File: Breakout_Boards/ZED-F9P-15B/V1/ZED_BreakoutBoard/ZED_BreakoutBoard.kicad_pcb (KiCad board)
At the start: 2 copper layers, 15 parts, among them IC1 ZED-F9P-15B, J1 RF2-04A-T-00-50-G, J2 GPS_Conn_02x04_Top_Bottom

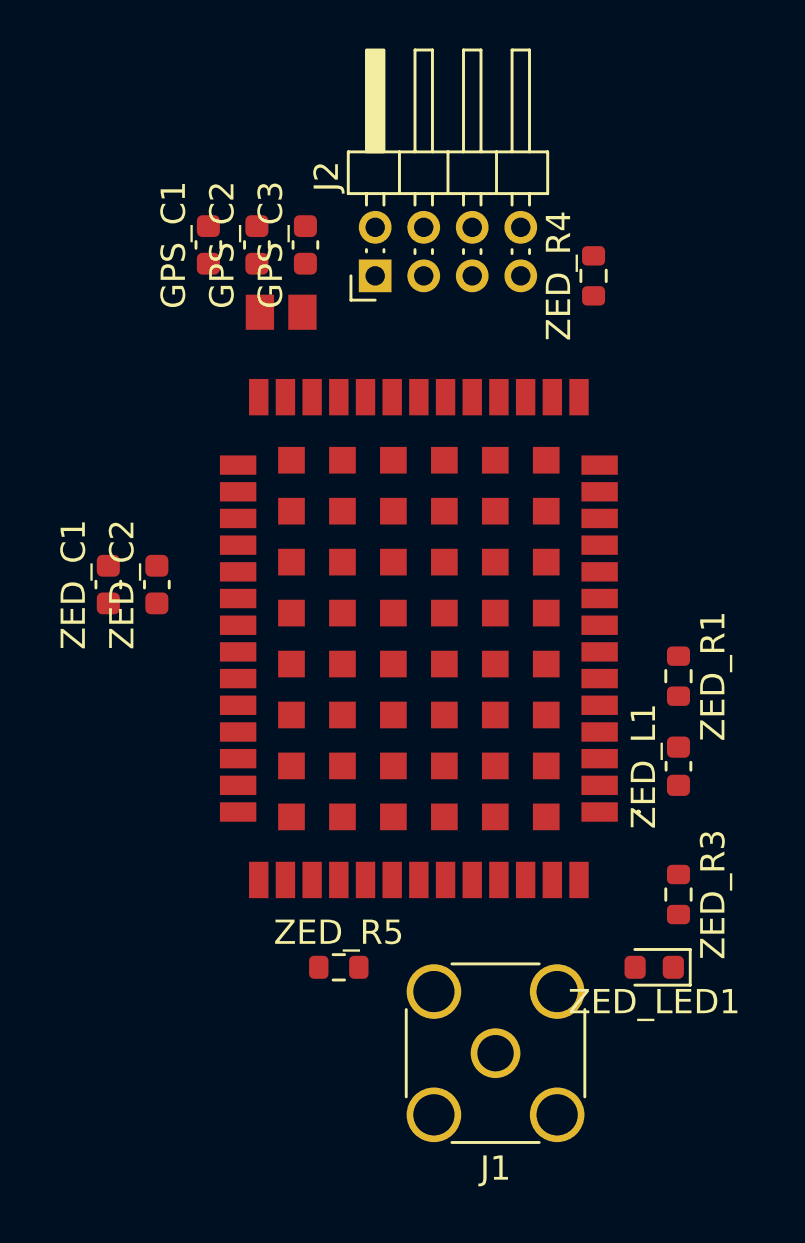
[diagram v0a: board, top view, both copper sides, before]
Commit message: fix: gnd connection, pcb approximative edge
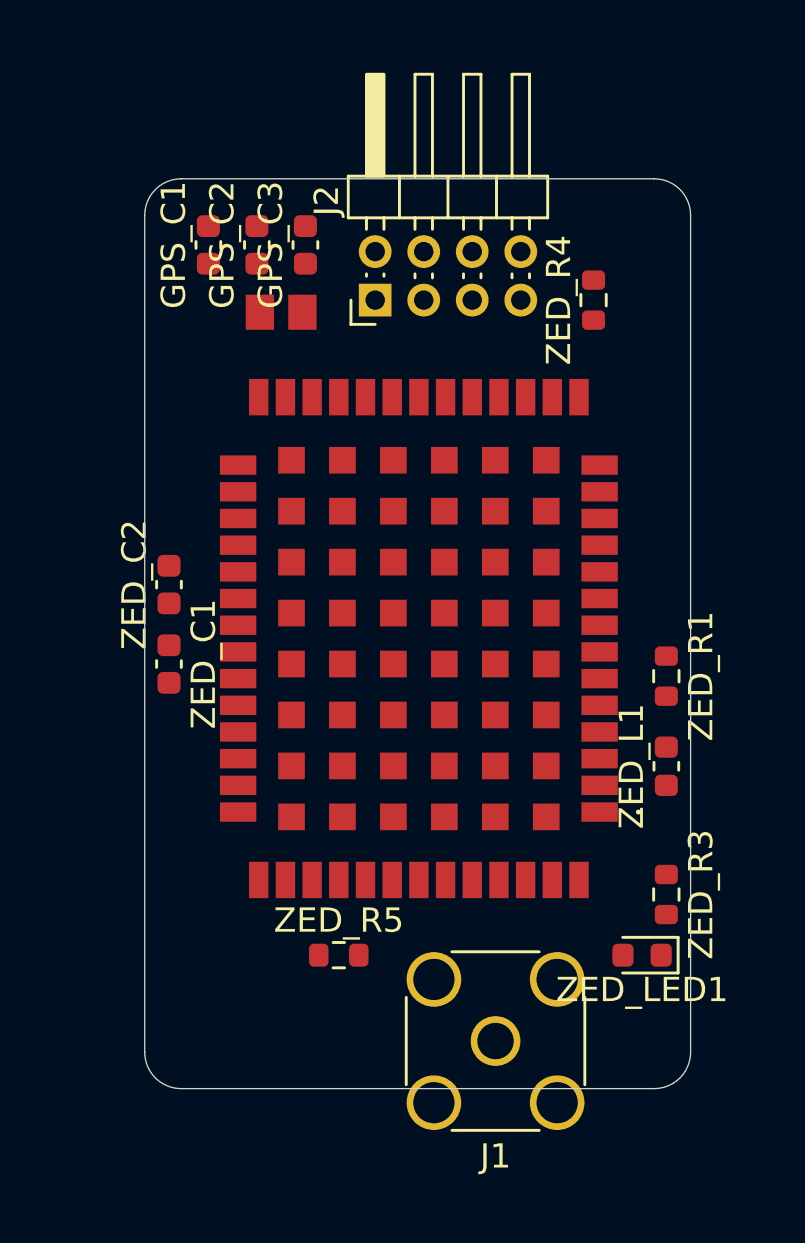
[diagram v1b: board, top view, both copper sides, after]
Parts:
- moved ZED_C1 4.12 mm to (122.0, 87.5), turned to -90 degrees
- moved J2 1.00 mm to (130.5, 72.5)
- moved ZED_R4 1.00 mm to (139.5, 72.5)
- moved ZED_LED1 0.71 mm to (141.5, 99.5)
- moved J1 0.50 mm to (135.5, 103.0)
- moved ZED_C2 0.50 mm to (122.0, 84.2)
- moved ZED_L1 0.50 mm to (142.5, 91.7)
- moved ZED_R1 0.50 mm to (142.5, 88.0)
- moved ZED_R3 0.50 mm to (142.5, 97.0)
- moved ZED_R5 0.50 mm to (129.0, 99.5)
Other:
- board outline added: 22.5 x 37.5 mm
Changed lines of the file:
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@@
 	(footprint "Resistor_SMD:R_0603_1608Metric"
 		(layer "F.Cu")
-		(at 129 100)
+		(at 129 99.5)
 		(descr "Resistor SMD 0603 (1608 Metric), square (rectangular) end terminal, IPC-7351 nominal, (Body size source: IPC-SM-782 page 72, https://www.pcb-3d.com/wordpress/wp-content/uploads/ipc-sm-782a_amendment_1_and_2.pdf), generated with kicad-footprint-generator")
 		(tags "resistor")
@@
 	(footprint "LED_SMD:LED_0603_1608Metric"
 		(layer "F.Cu")
-		(at 142 100 180)
+		(at 141.5 99.5 180)
 		(descr "LED SMD 0603 (1608 Metric), square (rectangular) end terminal, IPC-7351 nominal, (Body size source: http://www.tortai-tech.com/upload/download/2011102023233369053.pdf), generated with kicad-footprint-generator")
 		(tags "LED")
@@
 	(footprint "Resistor_SMD:R_0603_1608Metric"
 		(layer "F.Cu")
-		(at 143 97 -90)
+		(at 142.5 97 -90)
 		(descr "Resistor SMD 0603 (1608 Metric), square (rectangular) end terminal, IPC-7351 nominal, (Body size source: IPC-SM-782 page 72, https://www.pcb-3d.com/wordpress/wp-content/uploads/ipc-sm-782a_amendment_1_and_2.pdf), generated with kicad-footprint-generator")
 		(tags "resistor")
@@
 	(footprint "Resistor_SMD:R_0603_1608Metric"
 		(layer "F.Cu")
-		(at 143 88 -90)
+		(at 142.5 88 -90)
 		(descr "Resistor SMD 0603 (1608 Metric), square (rectangular) end terminal, IPC-7351 nominal, (Body size source: IPC-SM-782 page 72, https://www.pcb-3d.com/wordpress/wp-content/uploads/ipc-sm-782a_amendment_1_and_2.pdf), generated with kicad-footprint-generator")
 		(tags "resistor")
@@
 	(footprint "Connector_Coaxial:SMA_Wurth_60312002114503_Vertical"
 		(layer "F.Cu")
-		(at 135.46 103.54 180)
+		(at 135.46 103.04 180)
 		(descr "https://www.we-online.de/katalog/datasheet/60312002114503.pdf")
 		(tags "SMA THT Female Jack Vertical ExtendedLegs")
@@
 	(footprint "Inductor_SMD:L_0603_1608Metric"
 		(layer "F.Cu")
-		(at 143 91.7125 90)
+		(at 142.5 91.7125 90)
 		(descr "Inductor SMD 0603 (1608 Metric), square (rectangular) end terminal, IPC-7351 nominal, (Body size source: http://www.tortai-tech.com/upload/download/2011102023233369053.pdf), generated with kicad-footprint-generator")
 		(tags "inductor")
@@
 	(footprint "Capacitor_SMD:C_0603_1608Metric"
 		(layer "F.Cu")
-		(at 119.5 84.225 90)
+		(at 122 87.5 -90)
 		(descr "Capacitor SMD 0603 (1608 Metric), square (rectangular) end terminal, IPC-7351 nominal, (Body size source: IPC-SM-782 page 76, https://www.pcb-3d.com/wordpress/wp-content/uploads/ipc-sm-782a_amendment_1_and_2.pdf), generated with kicad-footprint-generator")
 		(tags "capacitor")
@@
 		(attr smd)
 		(fp_line
-			(start -0.14058 -0.51)
-			(end 0.14058 -0.51)
+			(start -0.14058 0.51)
+			(end 0.14058 0.51)
 			(stroke
 				(width 0.12)
@@
 		)
 		(fp_line
-			(start -0.14058 0.51)
-			(end 0.14058 0.51)
+			(start -0.14058 -0.51)
+			(end 0.14058 -0.51)
 			(stroke
 				(width 0.12)
@@
 		)
 		(fp_line
-			(start 1.48 -0.73)
-			(end 1.48 0.73)
+			(start -1.48 0.73)
+			(end -1.48 -0.73)
 			(stroke
 				(width 0.05)
@@
 		)
 		(fp_line
-			(start -1.48 -0.73)
-			(end 1.48 -0.73)
+			(start 1.48 0.73)
+			(end -1.48 0.73)
 			(stroke
 				(width 0.05)
@@
 		)
 		(fp_line
-			(start 1.48 0.73)
-			(end -1.48 0.73)
+			(start -1.48 -0.73)
+			(end 1.48 -0.73)
 			(stroke
 				(width 0.05)
@@
 		)
 		(fp_line
-			(start -1.48 0.73)
-			(end -1.48 -0.73)
+			(start 1.48 -0.73)
+			(end 1.48 0.73)
 			(stroke
 				(width 0.05)
@@
 		)
 		(fp_line
-			(start 0.8 -0.4)
-			(end 0.8 0.4)
+			(start -0.8 0.4)
+			(end -0.8 -0.4)
 			(stroke
 				(width 0.1)
@@
 		)
 		(fp_line
-			(start -0.8 -0.4)
-			(end 0.8 -0.4)
+			(start 0.8 0.4)
+			(end -0.8 0.4)
 			(stroke
 				(width 0.1)
@@
 		)
 		(fp_line
-			(start 0.8 0.4)
-			(end -0.8 0.4)
+			(start -0.8 -0.4)
+			(end 0.8 -0.4)
 			(stroke
 				(width 0.1)
@@
 		)
 		(fp_line
-			(start -0.8 0.4)
-			(end -0.8 -0.4)
+			(start 0.8 -0.4)
+			(end 0.8 0.4)
 			(stroke
 				(width 0.1)
@@
 		)
 		(pad "1" smd roundrect
-			(at -0.775 0 90)
+			(at -0.775 0 270)
 			(size 0.9 0.95)
 			(layers "F.Cu" "F.Mask" "F.Paste")
@@
 		)
 		(pad "2" smd roundrect
-			(at 0.775 0 90)
+			(at 0.775 0 270)
 			(size 0.9 0.95)
 			(layers "F.Cu" "F.Mask" "F.Paste")
@@
 	(footprint "Capacitor_SMD:C_0603_1608Metric"
 		(layer "F.Cu")
-		(at 121.5 84.225 90)
+		(at 122 84.225 90)
 		(descr "Capacitor SMD 0603 (1608 Metric), square (rectangular) end terminal, IPC-7351 nominal, (Body size source: IPC-SM-782 page 76, https://www.pcb-3d.com/wordpress/wp-content/uploads/ipc-sm-782a_amendment_1_and_2.pdf), generated with kicad-footprint-generator")
 		(tags "capacitor")
@@
 	(footprint "Connector_PinHeader_2.00mm:PinHeader_2x04_P2.00mm_Horizontal"
 		(layer "F.Cu")
-		(at 130.5 71.5 90)
+		(at 130.5 72.5 90)
 		(descr "Through hole angled pin header, 2x04, 2.00mm pitch, 4.2mm pin length, double rows")
 		(tags "Through hole angled pin header THT 2x04 2.00mm double row")
@@
 	(footprint "Resistor_SMD:R_0603_1608Metric"
 		(layer "F.Cu")
-		(at 139.5 71.5 90)
+		(at 139.5 72.5 90)
 		(descr "Resistor SMD 0603 (1608 Metric), square (rectangular) end terminal, IPC-7351 nominal, (Body size source: IPC-SM-782 page 72, https://www.pcb-3d.com/wordpress/wp-content/uploads/ipc-sm-782a_amendment_1_and_2.pdf), generated with kicad-footprint-generator")
 		(tags "resistor")
@@
 		)
 	)
+	(gr_arc
+		(start 122.5 105)
+		(mid 121.43934 104.56066)
+		(end 121 103.5)
+		(stroke
+			(width 0.05)
+			(type default)
+		)
+		(layer "Edge.Cuts")
+	)
+	(gr_line
+		(start 122.5 67.5)
+		(end 142 67.5)
+		(stroke
+			(width 0.05)
+			(type default)
+		)
+		(layer "Edge.Cuts")
+	)
+	(gr_line
+		(start 143.5 69)
+		(end 143.5 103.5)
+		(stroke
+			(width 0.05)
+			(type default)
+		)
+		(layer "Edge.Cuts")
+	)
+	(gr_arc
+		(start 121 69)
+		(mid 121.43934 67.93934)
+		(end 122.5 67.5)
+		(stroke
+			(width 0.05)
+			(type default)
+		)
+		(layer "Edge.Cuts")
+	)
+	(gr_line
+		(start 142 105)
+		(end 122.5 105)
+		(stroke
+			(width 0.05)
+			(type default)
+		)
+		(layer "Edge.Cuts")
+	)
+	(gr_arc
+		(start 143.5 103.5)
+		(mid 143.06066 104.56066)
+		(end 142 105)
+		(stroke
+			(width 0.05)
+			(type default)
+		)
+		(layer "Edge.Cuts")
+	)
+	(gr_arc
+		(start 142 67.5)
+		(mid 143.06066 67.93934)
+		(end 143.5 69)
+		(stroke
+			(width 0.05)
+			(type default)
+		)
+		(layer "Edge.Cuts")
+	)
+	(gr_line
+		(start 121 103.5)
+		(end 121 69)
+		(stroke
+			(width 0.05)
+			(type default)
+		)
+		(layer "Edge.Cuts")
+	)
 	(embedded_fonts no)

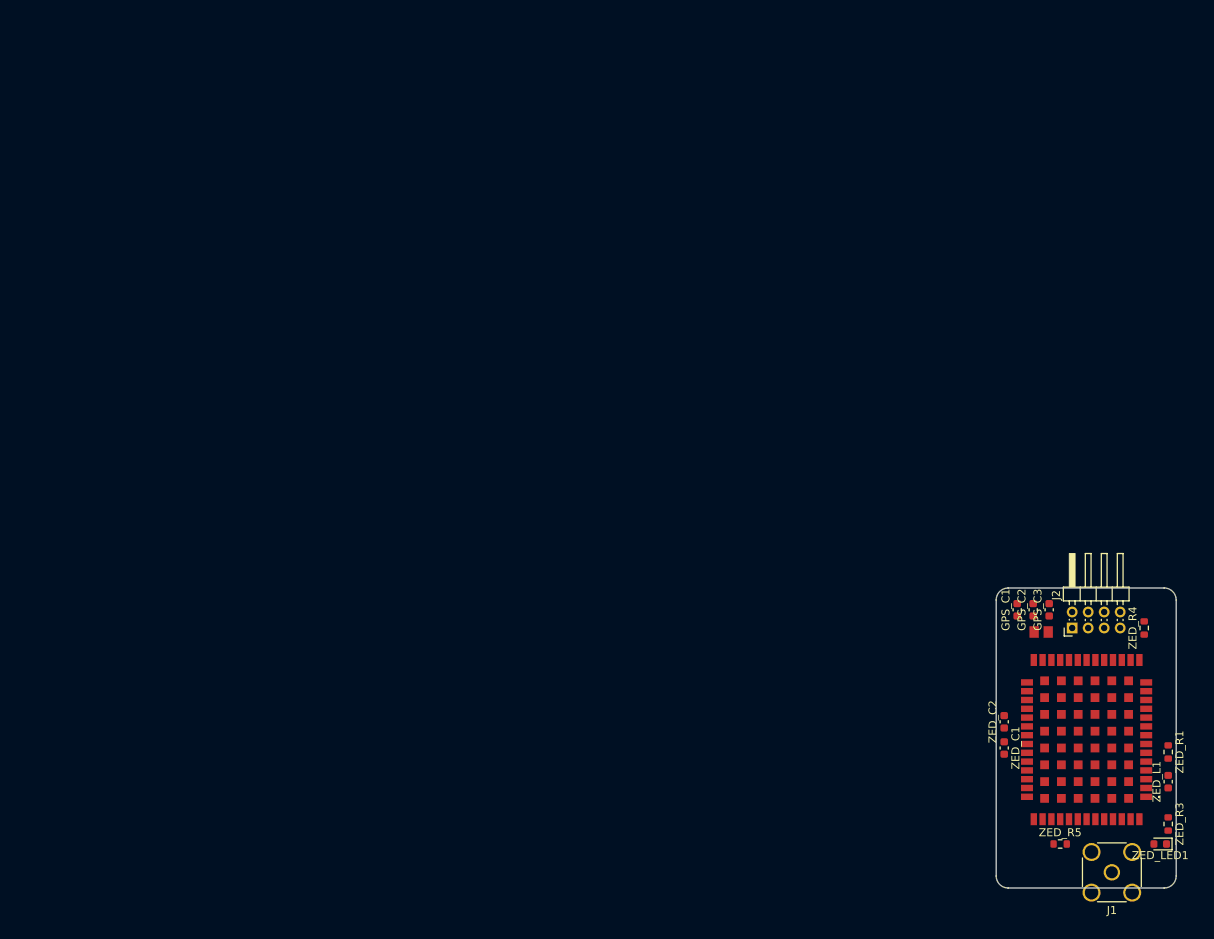
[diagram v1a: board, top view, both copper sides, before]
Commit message: feat edge pcb sma, add edge pcb layout
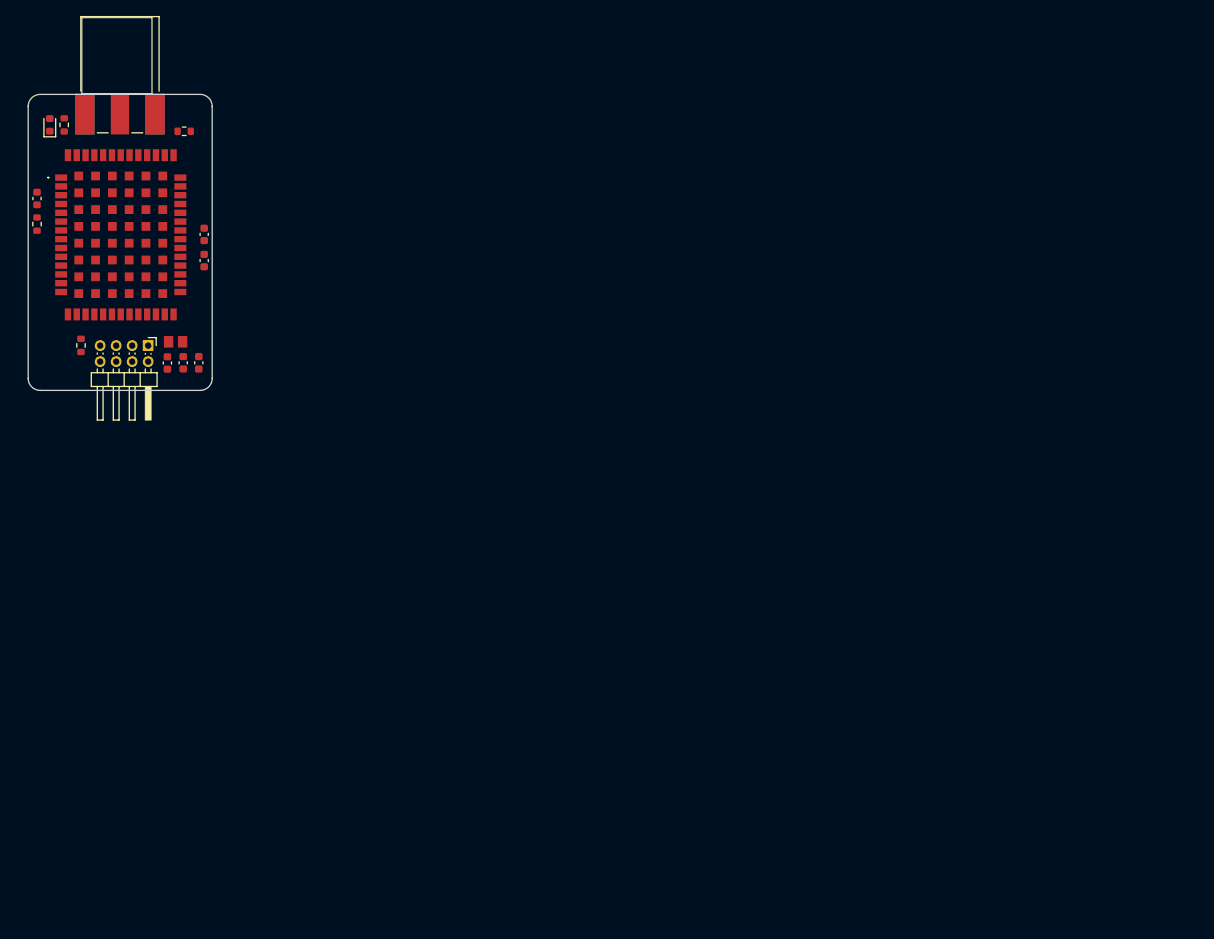
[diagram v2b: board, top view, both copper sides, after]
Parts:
- J1: value RF2-04A-T-00-50-G -> 142-0701-801; footprint Connector_Coaxial:SMA_Wurth_60312002114503_Vertical -> ZED_Library:CONN_142-0701-801
- moved ZED_LED1 165.4 mm to (2.70, 9.61), turned to 90 degrees
- moved ZED_R3 163.3 mm to (4.50, 9.61), turned to 90 degrees
- moved ZED_L1 159.1 mm to (1.10, 18.8), turned to -90 degrees
- moved J1 156.1 mm to (11.5, 8.27), turned to 0 degrees
- moved ZED_R1 156.0 mm to (1.10, 22.0), turned to 90 degrees
- moved ZED_R5 141.2 mm to (19.5, 10.4), turned to 180 degrees
- moved ZED_R4 137.5 mm to (6.60, 37.2), turned to -90 degrees
- moved IC1 136.2 mm to (11.6, 23.4), turned to -90 degrees
- moved J2 120.8 mm to (15.0, 37.2), turned to -90 degrees
- moved ZED_C1 118.8 mm to (22.0, 23.3), turned to 90 degrees
- moved ZED_C2 115.4 mm to (22.0, 26.6), turned to -90 degrees
- moved GPS_C3 114.5 mm to (17.4, 39.4), turned to -90 degrees
- moved GPS_FB1 114.1 mm to (18.4, 36.7), turned to 0 degrees
- moved GPS_C2 110.6 mm to (19.4, 39.4), turned to -90 degrees
- moved GPS_C1 106.9 mm to (21.3, 39.4), turned to -90 degrees
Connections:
- IC1 pad 49: GPS_GND -> Net-(IC1-RESET_N)
- J2 pad 6: ZED_EXTINT -> GPS_GND
- J2 pad 7: GPS_GND -> ZED_EXTINT
- J2 pad 8: GPS_GND -> Net-(J2-Pin_8)
- ZED_R4 pad 2: GPS_GND -> Net-(J2-Pin_8)
- ZED_R5 pad 2: GPS_GND -> Net-(IC1-RESET_N)
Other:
- board size 22.5 x 37.5 mm -> 23 x 37 mm
- board text added: "VCC"

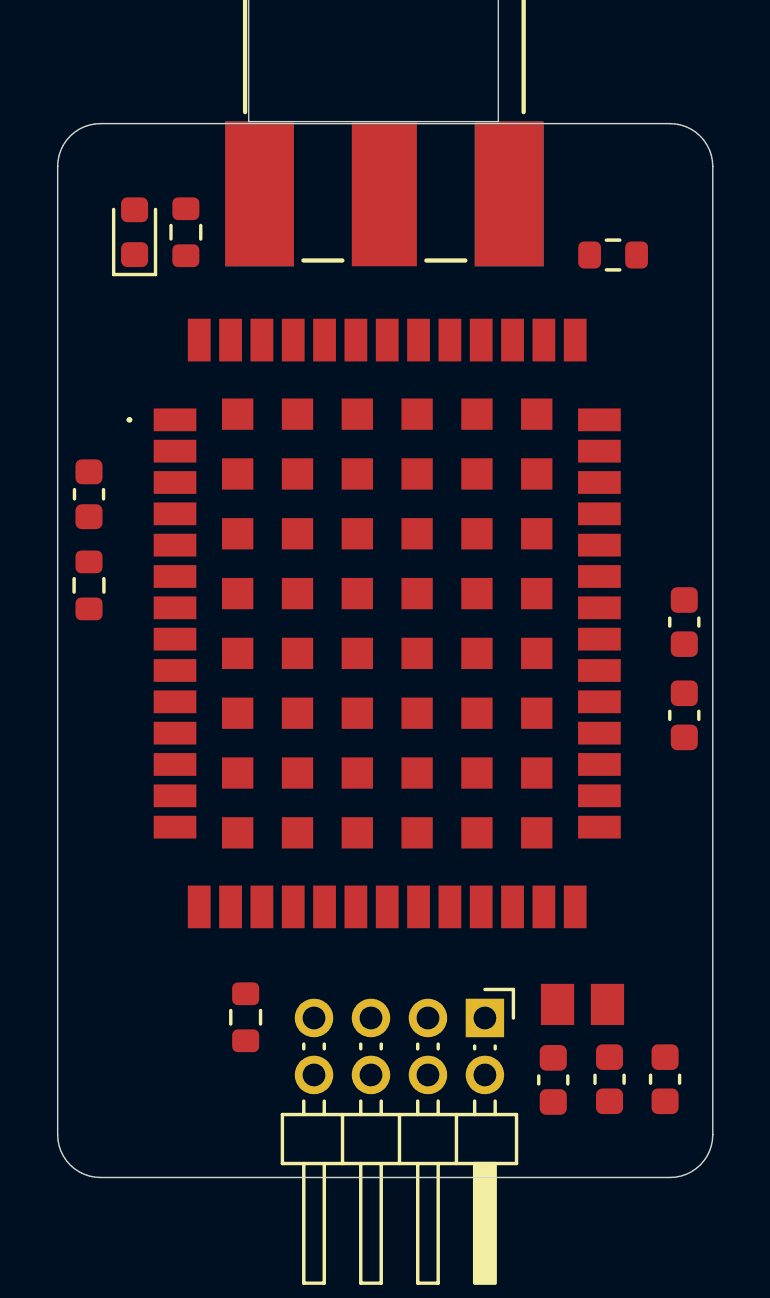
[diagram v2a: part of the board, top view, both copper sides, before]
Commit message: feat: add mounting holes M2 & cleanup unnecessary components & add sma footprint
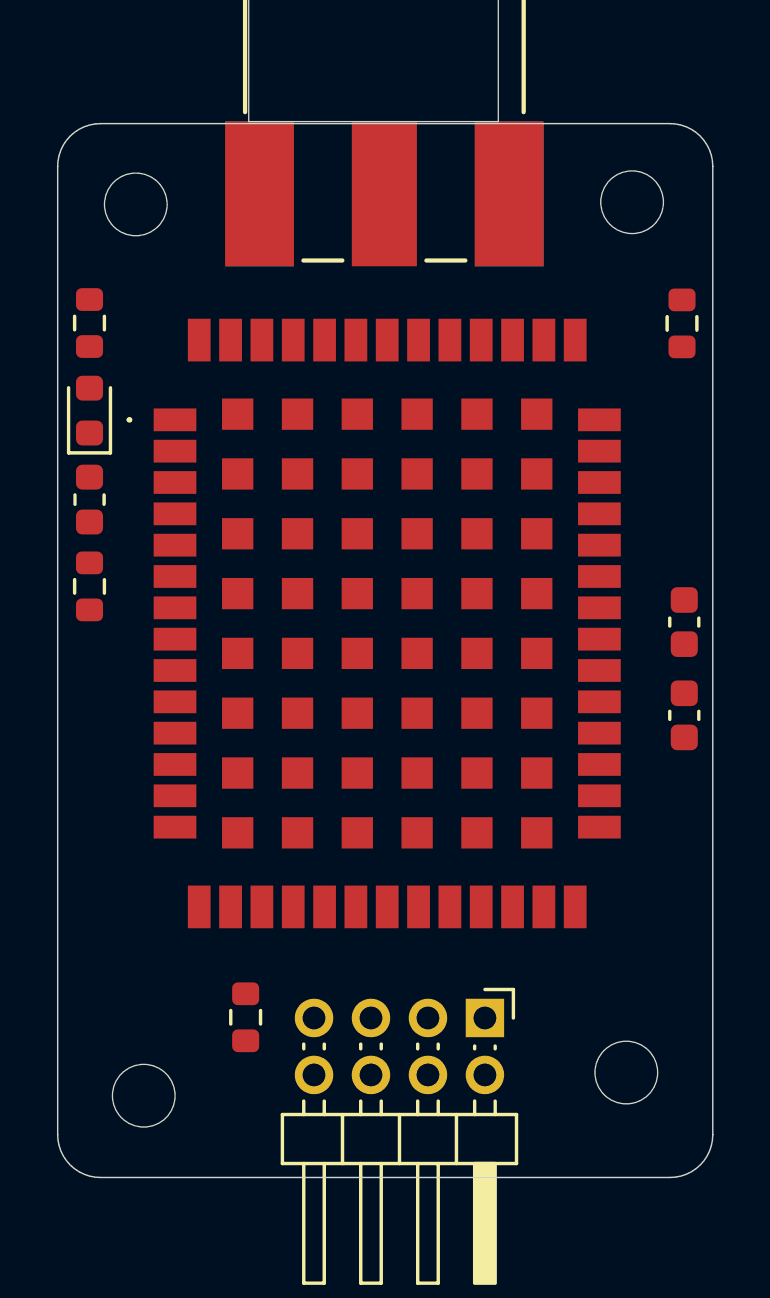
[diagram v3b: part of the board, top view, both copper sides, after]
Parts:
- removed GPS_C1: 100nF, Capacitor_SMD:C_0603_1608Metric
- removed GPS_C2, GPS_C3: 10uF, Capacitor_SMD:C_0603_1608Metric
- removed GPS_FB1: 120R, ZED_Library:IND_25_0805_FRT
- added H1: MountingHole, MountingHole:MountingHole_2.2mm_M2, F.Cu at (2.74, 8.64)
- added H2: MountingHole, MountingHole:MountingHole_2.2mm_M2, F.Cu at (20.2, 8.56)
- added H3: MountingHole, MountingHole:MountingHole_2.2mm_M2, F.Cu at (3.02, 39.9)
- added H4: MountingHole, MountingHole:MountingHole_2.2mm_M2, F.Cu at (20.0, 39.1)
- moved ZED_LED1 6.46 mm to (1.12, 15.9)
- moved ZED_R3 4.65 mm to (1.12, 12.8), turned to -90 degrees
- moved ZED_R5 3.41 mm to (21.9, 12.8), turned to 90 degrees
- moved ZED_L1 0.19 mm to (1.12, 19.0)
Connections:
- J2 pad 1: Net-(J2-Pin_1) -> GPS_VCC
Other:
- board text removed: "VCC"
